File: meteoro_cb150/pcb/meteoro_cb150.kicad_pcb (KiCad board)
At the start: 2 copper layers, 210 x 135 mm, 100 parts, among them J1 ENTRADA, Q1 MPSA92, Q2 MPSA92, Q3 BD139, Q4 BD140, Q5 BD139, Q6 2SA1943, Q7 2SC5200, Q8 MPSA42

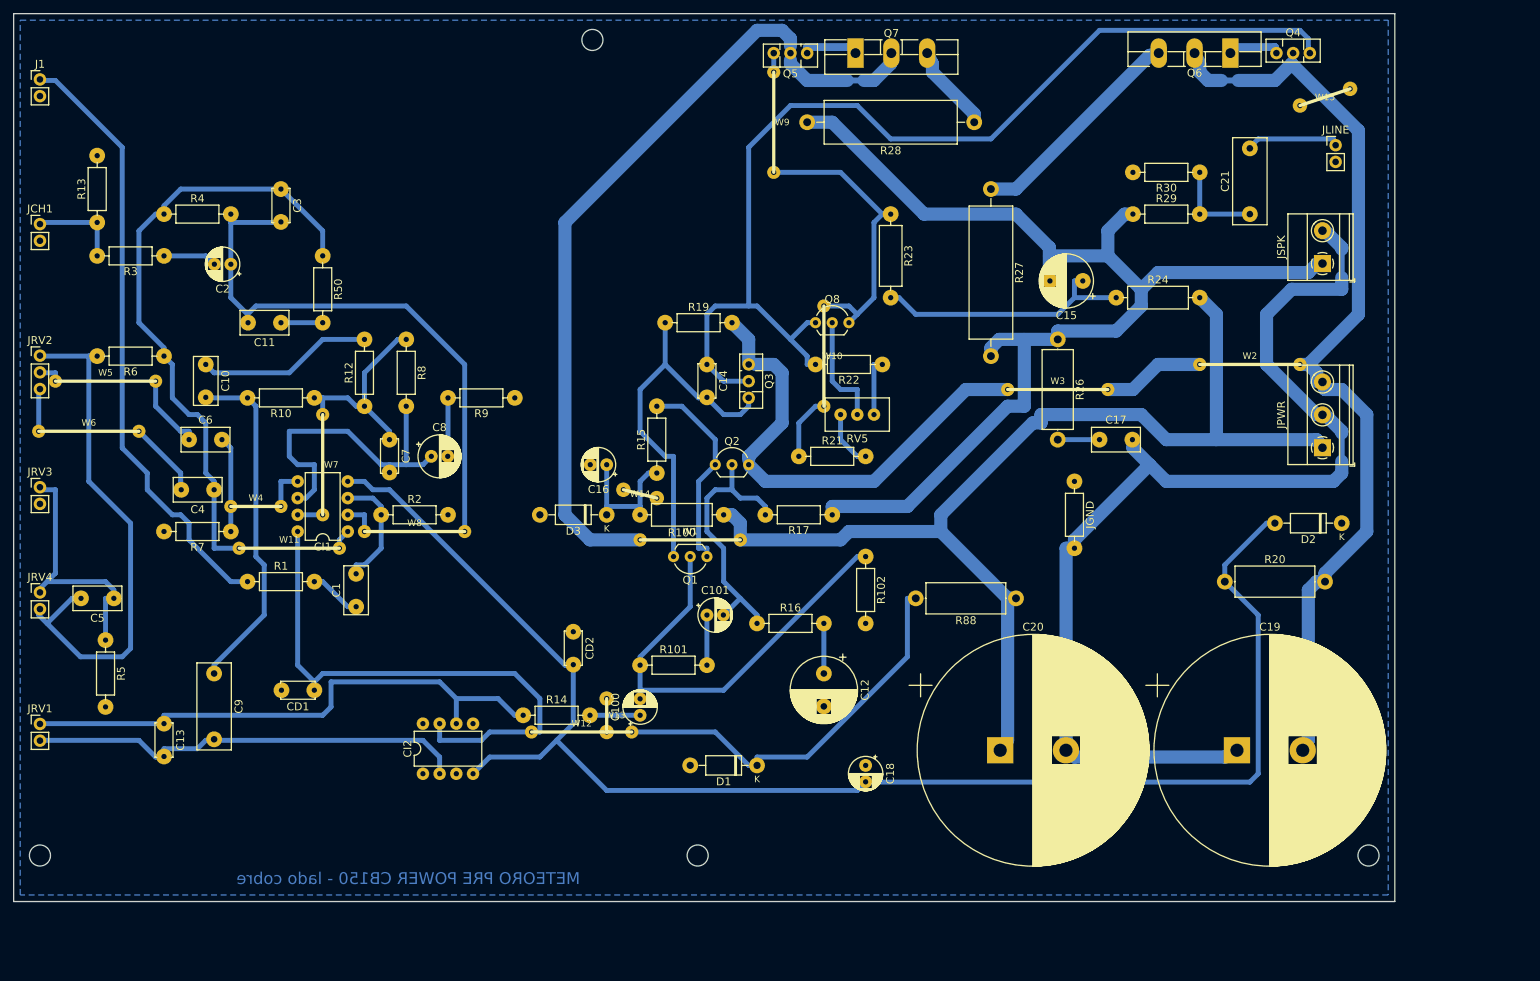
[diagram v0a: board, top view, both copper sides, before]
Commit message: Aplica melhorias ao Pre Power CB150 e refaz a placa em dupla face
Circuito: espelho de corrente e degeneracao no par diferencial, cauda
de 5,2 mA, limitadores de corrente na saida e no VAS, resistor entre
drivers, bobina de saida, offset equilibrado (R17 = R102), fusiveis nos
trilhos e filtros de 10000 uF. Simulado: distorcao 1 kHz/50 W 0,21% ->
0,06%, 20 kHz/140 W 11,6% -> 0,57%, curto na saida limitado a 8,5 A.

Placa: roteador com suporte a duas faces e vias; placa de 230 x 145 mm
sem jumpers (4 vias), DRC sem violacoes; PDF com as duas faces 1:1.

Co-Authored-By: Claude Opus 5.5 <noreply@anthropic.com>
Claude-Session: https://claude.ai/code/session_011MmAqYs34LARRMoPr44Zf6
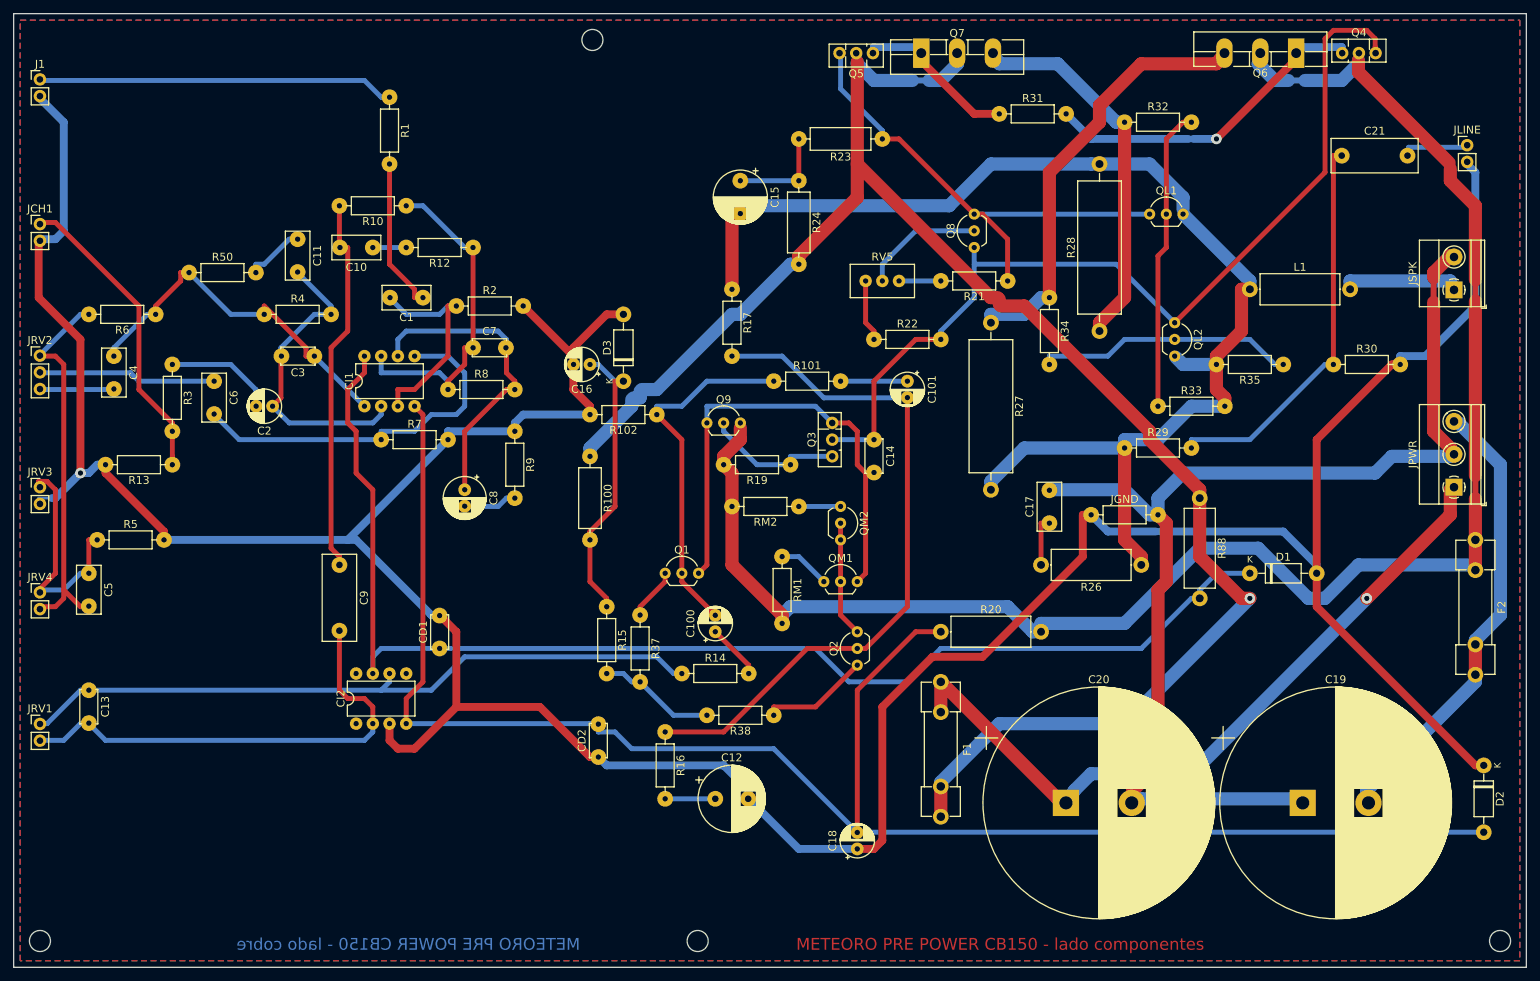
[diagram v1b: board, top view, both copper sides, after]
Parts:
- removed the ? at (24.0, 148.0)
- removed the ? at (124.0, 148.0)
- removed the ? at (226.0, 148.0)
- removed W1, W10, W11, W12, W13, W14, W15, W2, W3, W4, W5, W6, W7, W8, W9: jumper, 
- added ?: MountingHole_3.2mm_M3, MountingHole_3.2mm_M3, F.Cu at (24.0, 161.0)
- added ?: MountingHole_3.2mm_M3, MountingHole_3.2mm_M3, F.Cu at (246.0, 161.0)
- added ?: MountingHole_3.2mm_M3, MountingHole_3.2mm_M3, F.Cu at (124.0, 161.0)
- added F1: 5A rapido, Fuseholder_Clip-5x20mm_Littelfuse_100_Inline_P20.50x4.60mm_D1.30mm_Horizontal, F.Cu at (161.0, 121.6)
- added F2: 5A rapido, Fuseholder_Clip-5x20mm_Littelfuse_100_Inline_P20.50x4.60mm_D1.30mm_Horizontal, F.Cu at (242.2, 100.0)
- added L1: 10R 2W + 1uH, R_Axial_DIN0414_L11.9mm_D4.5mm_P15.24mm_Horizontal, F.Cu at (208.0, 61.9)
- added Q9: BC546, TO-92_Inline_Wide, F.Cu at (125.4, 82.2)
- added QL1: BC546, TO-92_Inline_Wide, F.Cu at (192.7, 50.5)
- added QL2: BC556, TO-92_Inline_Wide, F.Cu at (196.5, 67.0)
- added QM1: MPSA42, TO-92_Inline_Wide, F.Cu at (143.2, 106.4)
- added QM2: MPSA42, TO-92_Inline_Wide, F.Cu at (145.7, 94.9)
- added R31: 220R, R_Axial_DIN0207_L6.3mm_D2.5mm_P10.16mm_Horizontal, F.Cu at (169.9, 35.2)
- added R32: 3k3, R_Axial_DIN0207_L6.3mm_D2.5mm_P10.16mm_Horizontal, F.Cu at (188.9, 36.5)
- added R33: 1k, R_Axial_DIN0207_L6.3mm_D2.5mm_P10.16mm_Horizontal, F.Cu at (194.0, 79.7)
- added R34: 3k3, R_Axial_DIN0207_L6.3mm_D2.5mm_P10.16mm_Horizontal, F.Cu at (177.5, 63.2)
- added R35: 1k, R_Axial_DIN0207_L6.3mm_D2.5mm_P10.16mm_Horizontal, F.Cu at (213.0, 73.3)
- added R37: 47R, R_Axial_DIN0207_L6.3mm_D2.5mm_P10.16mm_Horizontal, F.Cu at (115.2, 111.4)
- added R38: 47R, R_Axial_DIN0207_L6.3mm_D2.5mm_P10.16mm_Horizontal, F.Cu at (135.6, 126.7)
- added RM1: 100R, R_Axial_DIN0207_L6.3mm_D2.5mm_P10.16mm_Horizontal, F.Cu at (136.8, 102.5)
- added RM2: 100R, R_Axial_DIN0207_L6.3mm_D2.5mm_P10.16mm_Horizontal, F.Cu at (139.4, 94.9)
- C19, C20: value 4700u/63V -> 10000u/63V
- R15: value 3k3 -> 1k6
- R16: value 120R -> 1k
- R17: value 3k3 -> 27k
- R19: value 560R -> 33R
- moved D1 80.4 mm to (208.0, 105.1), turned to 0 degrees
- moved R1 76.8 mm to (77.2, 32.7), turned to -90 degrees
- moved C15 54.3 mm to (130.5, 45.4), turned to -90 degrees
- moved R24 51.4 mm to (139.4, 45.4), turned to -90 degrees
- moved C1 48.1 mm to (82.2, 63.2), turned to 180 degrees
- moved R101 47.7 mm to (135.6, 75.9)
- moved C101 46.8 mm to (155.9, 75.9), turned to -90 degrees
- moved R20 43.8 mm to (161.0, 114.0)
- moved D2 42.7 mm to (243.5, 134.3), turned to -90 degrees
- moved R21 41.5 mm to (171.1, 60.6), turned to 180 degrees
- moved R13 38.6 mm to (44.1, 88.6), turned to 180 degrees
- moved R102 38.4 mm to (117.8, 81.0), turned to 180 degrees
- moved R17 37.5 mm to (129.2, 61.9), turned to -90 degrees
- moved Q2 37.4 mm to (148.3, 119.1), turned to 90 degrees
- moved R28 37.0 mm to (185.1, 68.3), turned to 90 degrees
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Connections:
- C19 pad 2: VN55 -> VN55R
- C20 pad 1: VP55 -> VP55R
- JPWR pad 1: VP55 -> VP55R
- JPWR pad 3: VN55 -> VN55R
- JSPK pad 1: OUT -> SPK
- Q1 pad 1: EDIF -> E1
- Q2 pad 1: EDIF -> E2
- Q2 pad 3: VN55 -> NM
- Q3 pad 1: VN55 -> E3
- R19 pad 1: VASB -> E3
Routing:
- net GND: track 0.00 -> 547.4 mm, vias 0 -> 1
- net VP55R: track 0.00 -> 112.4 mm, vias 0 -> 1
- net VN55R: track 0.00 -> 69.6 mm
- net FB: track 41.4 -> 105.9 mm
- net VP12: track 148.0 -> 197.0 mm
- net IN1N: track 94.2 -> 47.1 mm
- net LINE: track 14.0 -> 60.6 mm
- net QL1B: track 0.00 -> 46.0 mm
- net Q7E: track 13.3 -> 57.9 mm
- net Q6B: track 8.31 -> 50.7 mm, vias 0 -> 1
- net OUT1: track 98.4 -> 56.5 mm
- net QL2B: track 0.00 -> 39.5 mm
- net IN: track 93.3 -> 54.6 mm
- net VP55: track 296.6 -> 260.8 mm, vias 0 -> 1
- net IN1BP: track 20.9 -> 56.4 mm
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- added copper zone on F.Cu, net GND
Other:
- board size 210 x 135 mm -> 230 x 145 mm
- board text added: "METEORO PRE POWER CB150 - lado componentes"
